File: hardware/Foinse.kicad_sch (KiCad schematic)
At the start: 72 parts, among them J1 ESQ-110-X-X-D, J2 XT30PW-M, J4 PJ-002AH, J6 JTAG-10 PIN, U1 STM32F072C8Tx, U15 INA239AIDGSR, U16 INA239AIDGSR, U17 LTC4412xS6, U19 TPS56A37RPAR, U2 TLV70433DBVT, U4 TJA1051T-3, U5 TPS563203

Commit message: gonna
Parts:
- removed D10: BAT54C, Package_TO_SOT_SMD:SOT-23, symbol Diode:BAT54C
- C44, C45, C46: now fitted
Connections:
- net CAN_BUS+ is gone; now on net CAN_o+: D9.1 (K), R2.1, U4.7 (CANH)
- net CAN_BUS+- is gone; now on net CAN_o-: D9.2 (K), R1.2, U4.6 (CANL)
- net PA_+ is gone; now on net CAN_+: U1.33 (PA12)
- net PA_- is gone; now on net CAN_-: U1.32 (PA11)
- net 5VLOGIC: now also C10.1, U2.2 (IN)
- net VBAT: no longer D14.1 (K), MOSFET1.3 (S), U17.6 (SENSE)
- net CAN_RX renamed CAN_-
- net CAN_TX renamed CAN_+
- new net VBAT_BS?: D14.1 (K), MOSFET1.3 (S), U17.6 (SENSE)
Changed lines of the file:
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@@
 	)
 	(junction
+		(at 336.55 322.58)
+		(diameter 0)
+		(color 0 0 0 0)
+	)
+	(junction
 		(at 231.14 265.43)
 		(diameter 0)
@@
 	)
 	(junction
-		(at 340.36 322.58)
-		(diameter 0)
-		(color 0 0 0 0)
-	)
-	(junction
 		(at 408.94 248.92)
 		(diameter 0)
@@
 	(wire
 		(pts
-			(xy 340.36 322.58) (xy 342.9 322.58)
-		)
-		(stroke
-			(width 0)
-			(type default)
-		)
-	)
-	(wire
-		(pts
 			(xy 410.21 278.13) (xy 410.21 285.75)
 		)
@@
 	(wire
 		(pts
-			(xy 331.47 313.69) (xy 331.47 314.96)
-		)
-		(stroke
-			(width 0)
-			(type default)
-		)
-	)
-	(wire
-		(pts
 			(xy 231.14 254) (xy 231.14 255.27)
 		)
@@
 	(wire
 		(pts
-			(xy 347.98 313.69) (xy 347.98 307.34)
-		)
-		(stroke
-			(width 0)
-			(type default)
-		)
-	)
-	(wire
-		(pts
 			(xy 231.14 255.27) (xy 231.14 257.81)
 		)
@@
 	(wire
 		(pts
-			(xy 347.98 307.34) (xy 350.52 307.34)
-		)
-		(stroke
-			(width 0)
-			(type default)
-		)
-	)
-	(wire
-		(pts
 			(xy 224.79 102.87) (xy 224.79 104.14)
 		)
@@
 	(wire
 		(pts
-			(xy 340.36 318.77) (xy 340.36 322.58)
+			(xy 336.55 314.96) (xy 336.55 322.58)
 		)
 		(stroke
@@
 	(wire
 		(pts
-			(xy 332.74 313.69) (xy 331.47 313.69)
-		)
-		(stroke
-			(width 0)
-			(type default)
-		)
-	)
-	(wire
-		(pts
 			(xy 196.85 196.85) (xy 196.85 198.12)
 		)
@@
 	(wire
 		(pts
-			(xy 336.55 322.58) (xy 340.36 322.58)
+			(xy 336.55 322.58) (xy 342.9 322.58)
 		)
 		(stroke
@@
 	(global_label "5VLOGIC"
 		(shape input)
-		(at 350.52 307.34 0)
+		(at 336.55 314.96 0)
 		(fields_autoplaced yes)
 		(effects
@@
 		)
 		(property "Intersheetrefs" "${INTERSHEET_REFS}"
-			(at 361.3067 307.34 0)
+			(at 347.3367 314.96 0)
 			(effects
 				(font
@@
 		)
 	)
-	(global_label "PA_-"
+	(global_label "CAN_-"
 		(shape input)
 		(at 220.98 149.86 0)
@@
 		)
 		(property "Intersheetrefs" "${INTERSHEET_REFS}"
-			(at 228.8638 149.86 0)
+			(at 230.1943 149.86 0)
 			(effects
 				(font
@@
 		)
 	)
-	(global_label "CAN_BUS+"
+	(global_label "CAN_o+"
 		(shape input)
 		(at 422.003 182.1073 0)
@@
 		)
 		(property "Intersheetrefs" "${INTERSHEET_REFS}"
-			(at 435.0273 182.1073 0)
+			(at 432.3663 182.1073 0)
 			(effects
 				(font
@@
 		)
 	)
-	(global_label "CAN_TX"
+	(global_label "CAN_+"
 		(shape input)
 		(at 380.093 184.6473 180)
@@
 		)
 		(property "Intersheetrefs" "${INTERSHEET_REFS}"
-			(at 370.274 184.6473 0)
+			(at 370.8787 184.6473 0)
 			(effects
 				(font
@@
 		)
 	)
-	(global_label "VBAT"
+	(global_label "VBAT_BS?"
 		(shape input)
 		(at 304.8 162.56 180)
@@
 		)
 		(property "Intersheetrefs" "${INTERSHEET_REFS}"
-			(at 297.4 162.56 0)
+			(at 292.8643 162.56 0)
 			(effects
 				(font
@@
 		)
 	)
-	(global_label "VBUS_RAW"
-		(shape input)
-		(at 331.47 314.96 270)
-		(fields_autoplaced yes)
-		(effects
-			(font
-				(size 1.27 1.27)
-			)
-			(justify right)
-		)
-		(property "Intersheetrefs" "${INTERSHEET_REFS}"
-			(at 331.47 327.6214 90)
-			(effects
-				(font
-					(size 1.27 1.27)
-				)
-				(justify right)
-				(hide yes)
-			)
-		)
-	)
 	(global_label "NRST"
 		(shape input)
@@
 		)
 	)
-	(global_label "CAN_RX"
+	(global_label "CAN_-"
 		(shape input)
 		(at 380.093 187.1873 180)
@@
 		)
 		(property "Intersheetrefs" "${INTERSHEET_REFS}"
-			(at 369.9716 187.1873 0)
+			(at 370.8787 187.1873 0)
 			(effects
 				(font
@@
 		)
 	)
-	(global_label "CAN_BUS+-"
+	(global_label "CAN_o-"
 		(shape input)
 		(at 422.003 197.3473 0)
@@
 		)
 		(property "Intersheetrefs" "${INTERSHEET_REFS}"
-			(at 436.5997 197.3473 0)
+			(at 432.3663 197.3473 0)
 			(effects
 				(font
@@
 		)
 	)
-	(global_label "PA_+"
+	(global_label "CAN_+"
 		(shape input)
 		(at 220.98 152.4 0)
@@
 		)
 		(property "Intersheetrefs" "${INTERSHEET_REFS}"
-			(at 228.8638 152.4 0)
+			(at 230.1943 152.4 0)
 			(effects
 				(font
@@
 	)
 	(symbol
-		(lib_id "Diode:BAT54C")
-		(at 340.36 313.69 0)
-		(unit 1)
-		(exclude_from_sim no)
-		(in_bom yes)
-		(on_board yes)
-		(dnp no)
-		(fields_autoplaced yes)
-		(property "Reference" "D10"
-			(at 340.36 307.34 0)
-			(effects
-				(font
-					(size 1.27 1.27)
-				)
-			)
-		)
-		(property "Value" "BAT54C"
-			(at 340.36 309.88 0)
-			(effects
-				(font
-					(size 1.27 1.27)
-				)
-			)
-		)
-		(property "Footprint" "Package_TO_SOT_SMD:SOT-23"
-			(at 342.265 310.515 0)
-			(effects
-				(font
-					(size 1.27 1.27)
-				)
-				(justify left)
-				(hide yes)
-			)
-		)
-		(property "Datasheet" "http://www.diodes.com/_files/datasheets/ds11005.pdf"
-			(at 338.328 313.69 0)
-			(effects
-				(font
-					(size 1.27 1.27)
-				)
-				(hide yes)
-			)
-		)
-		(property "Description" "dual schottky barrier diode, common cathode"
-			(at 340.36 313.69 0)
-			(effects
-				(font
-					(size 1.27 1.27)
-				)
-				(hide yes)
-			)
-		)
-		(pin "1"
-		)
-		(pin "3"
-		)
-		(pin "2"
-		)
-		(instances
-			(project ""
-				(path "/e25e400c-9bc4-4e0b-8f6d-7db79788ea60"
-					(reference "D10")
-					(unit 1)
-				)
-			)
-		)
-	)
-	(symbol
 		(lib_id "power:GND")
 		(at 328.93 125.73 90)
@@
 		(in_bom yes)
 		(on_board yes)
-		(dnp yes)
+		(dnp no)
 		(property "Reference" "C46"
 			(at 312.42 240.03 0)
@@
 		(in_bom yes)
 		(on_board yes)
-		(dnp yes)
+		(dnp no)
 		(property "Reference" "C44"
 			(at 287.02 240.03 0)
@@
 		(in_bom yes)
 		(on_board yes)
-		(dnp yes)
+		(dnp no)
 		(property "Reference" "C45"
 			(at 299.72 240.03 0)

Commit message: give
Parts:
- removed C34, C35: 100nF, Capacitor_SMD:C_0402_1005Metric, symbol Device:C
- removed D14: D_Schottky, Package_TO_SOT_THT:TO-220-3_Vertical, symbol Device:D_Schottky
- removed J4: PJ-002AH, Foinse Footprints:PJ-002AH_CUD, symbol PJ-002AH:PJ-002AH
- removed R45, R46: 10 mΩ, Resistor_SMD:R_0402_1005Metric, symbol Device:R
- removed U15, U16: INA239AIDGSR, Foinse Footprints:VSSOP_9AIDGST_TEX, symbol INA239:INA239AIDGSR
- added C23, C24: 100nF, Capacitor_SMD:C_0402_1005Metric, symbol Device:C
- added C25, C26: 100nf, Capacitor_SMD:C_0402_1005Metric, symbol Device:C
- added D1: SR1020, footprints:TO254P1050X476X2020-3, symbol SR1020:SR1020
- added J3: PJ-063AH, footprints:CUI_PJ-063AH, symbol PJ-063AH:PJ-063AH
- added R7: 35kΩ, Resistor_SMD:R_0402_1005Metric, symbol Device:R
- added U6, U7: ACS71240KEXBLT-010B3, QFN12_ACS711KEXLT-31AB-T_ALM, symbol ACS71240KEXBLT:ACS71240KEXBLT-030B3
- R50: value 3.3k Ω -> 3.3kΩ
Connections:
- net 5V_LOGIC is gone; now on net 5VLOGIC: J1.05, J1.06
- net 3.3V: now also C23.2, C24.2, U6.12, U7.12
- net 5VSERVO: now also J1.01, J1.02, U7.1, U7.2
- net GND: now also C23.1, C24.1, C25.2, C26.2, J3.2, J3.S1 (SHIELD), J3.S2 (SHIELD), R7.1, U6.5, U7.5
- net at J2.P, MOSFET1.2 (D), U17.1 (VIN): now also C26.1
- net Fault2: now reaches R6.1, U19.4 (PG)
- net Fault2: now also U7.6
- net Fault1: now reaches R3.2, U5.5 (EN)
- net Fault1: now also R7.2, U6.6
- net Sense1: now reaches U1.13 (PA3)
- net Sense1: now also U6.11
- net Sense2: now reaches U1.14 (PA4)
- net Sense2: now also U7.11
- net 5VSERVO_BS renamed 5VSERVO_S
- net 5VSERVO_S: now also U7.3, U7.4; no longer J1.01, J1.02
- net SPI_CLK: no longer names the net of U1.15 (PA5)
- net SPI_MISO: no longer names the net of U1.16 (PA6)
- net SPI_MOSI: no longer names the net of U1.17 (PA7)
- net VBAT renamed pwr
- net pwr: now also U6.3, U6.4
- net VBAT_BS? renamed pwr_s
- net pwr_s: now also C25.1, D1.2, U6.1, U6.2
- new net: D1.1, D1.3, J3.1
- no-connect marks 10 -> 45
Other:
- note removed: "what is the current and voltage rating for this?"
- moved on the sheet: C10, C11, C16, C17, C18, C19, C20, C21, C22, C36, C37, C38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

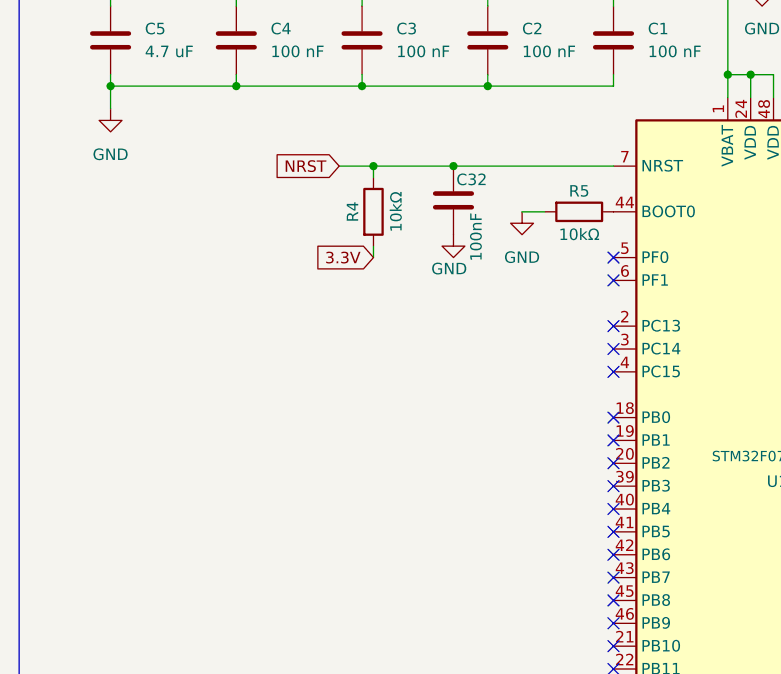
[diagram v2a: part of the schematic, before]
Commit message: can crystal added
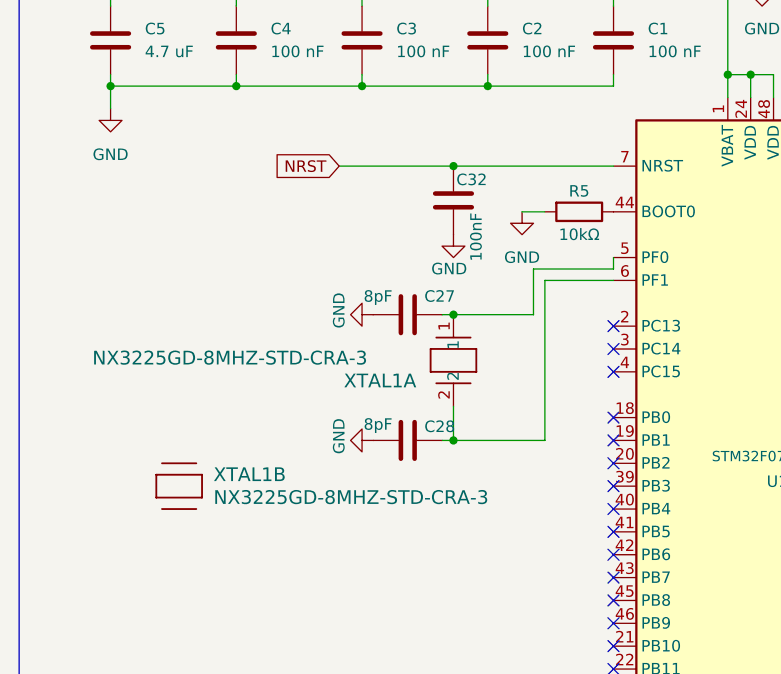
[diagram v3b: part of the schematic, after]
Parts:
- removed R4: 10kΩ, Resistor_SMD:R_0402_1005Metric, symbol Device:R
- added C27, C28: 8pF, Capacitor_SMD:C_0402_1005Metric, symbol Device:C
- added XTAL1: NX3225GD-8MHZ-STD-CRA-3, XTAL_NX3225GD-8MHZ-STD-CRA-3_NDK, symbol STDCRA38M:NX3225GD-8MHZ-STD-CRA-3
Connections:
- net GND: now also C27.1, C28.2
- net at U1.5 (PF0): now also C27.2, XTAL1.1
- net at U1.6 (PF1): now also C28.1, XTAL1.2
- no-connect marks 45 -> 43

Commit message: lots to do
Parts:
- removed D1: SR1020, footprints:TO254P1050X476X2020-3, symbol SR1020:SR1020
- removed J2: XT30PW-M, footprints:AMASS_XT30PW-M, symbol XT30PW-M:XT30PW-M
- removed J6: JTAG-10 PIN, Connector_IDC:IDC-Header_2x05_P2.54mm_Vertical, symbol Connector_Generic_MountingPin:Conn_01x10_MountingPin
- removed MOSFET1: IPP80P03P4L04AKSA1, Foinse Footprints:IPP80P03P4L04AKSA1, symbol IPP80P03P4L04AKSA1:IPP80P03P4L04AKSA1
- added D2: BAT54C, Package_TO_SOT_SMD:SOT-23, symbol Diode:BAT54C
- added J10, J11, J12, J13, J14, J16, J2, J5, J6, J7, J8, J9: S2761-46R, HARWIN_S2761-46R, symbol S2761-46R:S2761-46R
- added J15: 39-29-1048, MOLEX_39-29-1048, symbol 39-29-1048:39-29-1048
- added J4: 5023860570, MOLEX_5023860570, symbol 5023860570:5023860570
- added Q1, Q2: IPD90P04P4L04ATMA1, PG-TO252-3-313_INF, symbol IPD90P04P4L04ATMA1:IPD90P04P4L04ATMA1
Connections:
- net 3.3V: now also J4.4, J5.1
- net 5VLOGIC: now also J1.11, J1.12, J10.1; no longer J1.05, J1.06
- net 5VSERVO: now also J1.03, J1.04, J1.05, J1.06, J1.07, J1.08; no longer J1.01, J1.02
- net 5VSERVO_S: now also J9.1
- net CAN_o+: now also J12.1
- net CAN_o-: now also J11.1
- net Fault1: now also J8.1
- net Fault2: now also J7.1
- net GND: now also J1.01, J1.02, J1.09, J1.10, J1.13, J1.15, J1.17, J15.3, J15.4, J16.1, J4.5, J4.S1 (SHIELD1), J4.S2 (SHIELD2), J6.1, Q2.1 (G); no longer J1.03, J1.04, J1.07, J1.08
- net NRST: now also J4.3; no longer J1.17
- net SWDIO: now also J4.2; no longer J1.15
- net Sense1: now also J13.1
- net Sense2: now also J14.1
- net pwr_s: now also Q1.3 (S), Q2.3 (S)
- net at J3.1: now also Q2.2 (D)
- net at U17.5 (GATE): now also Q1.1 (G)
- net at C26.1, U17.1 (VIN): now also J15.1, J15.2, Q1.2 (D)
- net SWCLK3 renamed SWCLK
- net SWCLK: now also J4.1; no longer J1.11
- new net 3.3V_Dig: J2.1
- new net 5V_LOGIC: D2.2
- new net VBAT_Local: D2.1
- new net power/vin: D2.3
- no-connect marks 43 -> 35
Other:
- added sheet power (power.kicad_sch)
- note removed: "Connector_IDC:IDC-Header_2x05_P2.54mm_Vertical"
- moved on the sheet: C12, C13, C14, C15, D9, J3, R1, R2, R5, U4

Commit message: minor stuff
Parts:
- removed C10: 100nF, Capacitor_SMD:C_0402_1005Metric, symbol Device:C
- removed C11: 1 uF, Capacitor_SMD:C_0402_1005Metric, symbol Device:C
- removed D2: BAT54C, Package_TO_SOT_SMD:SOT-23, symbol Diode:BAT54C
- removed J5, J6: S2761-46R, HARWIN_S2761-46R, symbol S2761-46R:S2761-46R
- removed U2: TLV70433DBVT, Foinse Footprints:DBV0005A_N, symbol TLV70433DBVT:TLV70433DBVT
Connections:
- net 3.3V_Dig is gone; now on net 3.3V: J2.1
- net 5VLOGIC: now also R50.2; no longer R50.1
- net at D12.2 (A): now also R50.1; no longer R50.2
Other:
- moved on the sheet: J16, J2, R50

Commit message: minor changes
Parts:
- 3V3: renamed from J2; value S2761-46R -> 3V3
- 5VLOGIC1: renamed from J10; value S2761-46R -> 5vLogic
- GND1: renamed from J16; value S2761-46R -> GND
- J7: value S2761-46R -> FAULT2
- J8: value S2761-46R -> FAULT1
- renumbered J9 to 5VSERVO1, J12 to CAN+1, J11 to CAN-1, J13 to SENSE1, J14 to SENSE2
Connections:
- net 5VSERVO: now also U7.3, U7.4; no longer U7.1, U7.2
- net 5VSERVO_S: now also U7.1, U7.2; no longer U7.3, U7.4
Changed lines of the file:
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@@
 		)
 	)
+	(text_box ""
+		(exclude_from_sim no)
+		(at 326.39 294.64 0)
+		(size 80.01 41.91)
+		(margins 0.9525 0.9525 0.9525 0.9525)
+		(stroke
+			(width 0)
+			(type solid)
+		)
+		(fill
+			(type none)
+		)
+		(effects
+			(font
+				(size 1.27 1.27)
+			)
+			(justify left top)
+		)
+	)
 	(junction
 		(at 294.64 317.5)
@@
 	(wire
 		(pts
+			(xy 204.47 317.5) (xy 207.01 317.5)
+		)
+		(stroke
+			(width 0)
+			(type default)
+		)
+	)
+	(wire
+		(pts
 			(xy 414.4825 180.8373) (xy 414.383 180.8373)
 		)
@@
 	(wire
 		(pts
-			(xy 207.01 313.69) (xy 207.01 317.5)
-		)
-		(stroke
-			(width 0)
-			(type default)
-		)
-	)
-	(wire
-		(pts
 			(xy 179.07 259.08) (xy 170.18 259.08)
 		)
@@
 		)
 	)
-	(global_label "pwr_s"
+	(global_label "5VSERVO"
 		(shape input)
-		(at 299.72 156.21 180)
+		(at 345.44 270.51 180)
 		(fields_autoplaced yes)
 		(effects
@@
 		)
 		(property "Intersheetrefs" "${INTERSHEET_REFS}"
-			(at 291.4734 156.21 0)
+			(at 334.1091 270.51 0)
 			(effects
 				(font
@@
 		)
 	)
-	(global_label "NRST"
+	(global_label "pwr_s"
 		(shape input)
-		(at 148.59 121.92 180)
+		(at 299.72 156.21 180)
 		(fields_autoplaced yes)
 		(effects
@@
 		)
 		(property "Intersheetrefs" "${INTERSHEET_REFS}"
-			(at 140.8272 121.92 0)
+			(at 291.4734 156.21 0)
 			(effects
 				(font
@@
 		)
 	)
-	(global_label "5VSERVO"
+	(global_label "NRST"
 		(shape input)
-		(at 345.44 264.16 180)
+		(at 148.59 121.92 180)
 		(fields_autoplaced yes)
 		(effects
@@
 		)
 		(property "Intersheetrefs" "${INTERSHEET_REFS}"
-			(at 334.1091 264.16 0)
+			(at 140.8272 121.92 0)
 			(effects
 				(font
@@
 		)
 	)
-	(global_label "5VSERVO_S"
-		(shape input)
-		(at 345.44 271.78 180)
-		(fields_autoplaced yes)
-		(effects
-			(font
-				(size 1.27 1.27)
-			)
-			(justify right)
-		)
-		(property "Intersheetrefs" "${INTERSHEET_REFS}"
-			(at 331.932 271.78 0)
-			(effects
-				(font
-					(size 1.27 1.27)
-				)
-				(justify right)
-				(hide yes)
-			)
-		)
-	)
 	(global_label "CAN_-"
 		(shape input)
@@
 	(global_label "pwr"
 		(shape input)
-		(at 207.01 313.69 90)
+		(at 204.47 317.5 180)
 		(fields_autoplaced yes)
 		(effects
@@
 				(size 1.27 1.27)
 			)
-			(justify left)
+			(justify right)
 		)
 		(property "Intersheetrefs" "${INTERSHEET_REFS}"
-			(at 207.01 307.4391 90)
+			(at 198.2191 317.5 0)
 			(effects
 				(font
 					(size 1.27 1.27)
 				)
-				(justify left)
+				(justify right)
 				(hide yes)
 			)
@@
 	(global_label "5VSERVO_S"
 		(shape input)
+		(at 345.44 265.43 180)
+		(fields_autoplaced yes)
+		(effects
+			(font
+				(size 1.27 1.27)
+			)
+			(justify right)
+		)
+		(property "Intersheetrefs" "${INTERSHEET_REFS}"
+			(at 331.932 265.43 0)
+			(effects
+				(font
+					(size 1.27 1.27)
+				)
+				(justify right)
+				(hide yes)
+			)
+		)
+	)
+	(global_label "5VSERVO_S"
+		(shape input)
 		(at 313.69 238.76 90)
 		(fields_autoplaced yes)
@@
 		(on_board yes)
 		(dnp no)
-		(property "Reference" "J9"
+		(property "Reference" "5VSERVO1"
 			(at 297.688 234.188 0)
 			(effects
@@
 			(project "Foinse"
 				(path "/e25e400c-9bc4-4e0b-8f6d-7db79788ea60"
-					(reference "J9")
+					(reference "5VSERVO1")
 					(unit 1)
 				)
@@
 		(dnp no)
 		(fields_autoplaced yes)
-		(property "Reference" "J2"
+		(property "Reference" "3V3"
 			(at 378.46 316.2299 90)
 			(effects
@@
 			)
 		)
-		(property "Value" "S2761-46R"
+		(property "Value" "3V3"
 			(at 378.46 318.7699 90)
 			(effects
@@
 			(project "Foinse"
 				(path "/e25e400c-9bc4-4e0b-8f6d-7db79788ea60"
-					(reference "J2")
+					(reference "3V3")
 					(unit 1)
 				)
@@
 		(dnp no)
 		(fields_autoplaced yes)
-		(property "Reference" "J16"
+		(property "Reference" "GND1"
 			(at 378.46 326.3899 90)
 			(effects
@@
 			)
 		)
-		(property "Value" "S2761-46R"
+		(property "Value" "GND"
 			(at 378.46 328.9299 90)
 			(effects
@@
 			(project "Foinse"
 				(path "/e25e400c-9bc4-4e0b-8f6d-7db79788ea60"
-					(reference "J16")
+					(reference "GND1")
 					(unit 1)
 				)
@@
 		(on_board yes)
 		(dnp no)
-		(property "Reference" "J13"
+		(property "Reference" "SENSE1"
 			(at 225.552 123.698 0)
 			(effects
@@
 			(project "Foinse"
 				(path "/e25e400c-9bc4-4e0b-8f6d-7db79788ea60"
-					(reference "J13")
+					(reference "SENSE1")
 					(unit 1)
 				)
@@
 		(on_board yes)
 		(dnp no)
-		(property "Reference" "J12"
+		(property "Reference" "CAN+1"
 			(at 426.212 175.768 0)
 			(effects
@@
 			(project "Foinse"
 				(path "/e25e400c-9bc4-4e0b-8f6d-7db79788ea60"
-					(reference "J12")
+					(reference "CAN+1")
 					(unit 1)
 				)
@@
 		(on_board yes)
 		(dnp no)
-		(property "Reference" "J10"
+		(property "Reference" "5VLOGIC1"
 			(at 302.768 310.388 0)
 			(effects
@@
 			)
 		)
-		(property "Value" "S2761-46R"
+		(property "Value" "5vLogic"
 			(at 305.308 315.976 0)
 			(effects
@@
 			(project "Foinse"
 				(path "/e25e400c-9bc4-4e0b-8f6d-7db79788ea60"
-					(reference "J10")
+					(reference "5VLOGIC1")
 					(unit 1)
 				)
@@
 			)
 		)
-		(property "Value" "S2761-46R"
+		(property "Value" "FAULT1"
 			(at 341.122 246.634 0)
 			(effects
@@
 			)
 		)
-		(property "Value" "S2761-46R"
+		(property "Value" "FAULT2"
 			(at 342.392 278.384 0)
 			(effects
@@
 		(on_board yes)
 		(dnp no)
-		(property "Reference" "J14"
+		(property "Reference" "SENSE2"
 			(at 225.552 136.398 0)
 			(effects
@@
 			(project "Foinse"
 				(path "/e25e400c-9bc4-4e0b-8f6d-7db79788ea60"
-					(reference "J14")
+					(reference "SENSE2")
 					(unit 1)
 				)
@@
 		(on_board yes)
 		(dnp no)
-		(property "Reference" "J11"
+		(property "Reference" "CAN-1"
 			(at 424.942 202.438 0)
 			(effects
@@
 			(project "Foinse"
 				(path "/e25e400c-9bc4-4e0b-8f6d-7db79788ea60"
-					(reference "J11")
+					(reference "CAN-1")
 					(unit 1)
 				)

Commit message: minor changes
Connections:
- net BATTERY_CURRENT_CS: no longer names the net of U1.27 (PB14)
- net SERVO_CURRENT_CS: no longer names the net of U1.28 (PB15)
- no-connect marks 35 -> 37
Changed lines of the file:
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@@
 	)
 	(no_connect
+		(at 179.07 187.96)
+	)
+	(no_connect
 		(at 179.07 175.26)
 	)
@@
 	)
 	(no_connect
+		(at 179.07 185.42)
+	)
+	(no_connect
 		(at 386.08 269.24)
 	)
@@
 	(wire
 		(pts
-			(xy 172.72 185.42) (xy 179.07 185.42)
-		)
-		(stroke
-			(width 0)
-			(type default)
-		)
-	)
-	(wire
-		(pts
 			(xy 224.79 113.03) (xy 224.79 115.57)
 		)
@@
 	(wire
 		(pts
-			(xy 172.72 187.96) (xy 179.07 187.96)
-		)
-		(stroke
-			(width 0)
-			(type default)
-		)
-	)
-	(wire
-		(pts
 			(xy 151.13 102.87) (xy 165.1 102.87)
 		)
@@
 		)
 	)
-	(global_label "SERVO_CURRENT_CS"
-		(shape input)
-		(at 172.72 187.96 180)
-		(fields_autoplaced yes)
-		(effects
-			(font
-				(size 1.27 1.27)
-			)
-			(justify right)
-		)
-		(property "Intersheetrefs" "${INTERSHEET_REFS}"
-			(at 150.6849 187.96 0)
-			(effects
-				(font
-					(size 1.27 1.27)
-				)
-				(justify right)
-				(hide yes)
-			)
-		)
-	)
 	(global_label "CAN_-"
 		(shape input)
@@
 		)
 	)
-	(global_label "5V_LOGIC"
+	(global_label "5VLOGIC"
 		(shape input)
 		(at 345.44 312.42 180)
@@
 		)
 		(property "Intersheetrefs" "${INTERSHEET_REFS}"
-			(at 333.6857 312.42 0)
+			(at 334.6533 312.42 0)
 			(effects
 				(font
@@
 				(hide yes)
 			)
-		)
-	)
-	(global_label "BATTERY_CURRENT_CS"
-		(shape input)
-		(at 172.72 185.42 180)
-		(fields_autoplaced yes)
-		(effects
-			(font
-				(size 1.27 1.27)
-			)
-			(justify right)
-		)
-		(property "Intersheetrefs" "${INTERSHEET_REFS}"
-			(at 148.9311 185.42 0)
-			(effects
-				(font
-					(size 1.27 1.27)
-				)
-				(justify right)
-				(hide yes)
-			)
